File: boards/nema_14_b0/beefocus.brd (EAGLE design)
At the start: 82.2 x 44.4 mm, 24 parts, among them J3 POWER_JACK

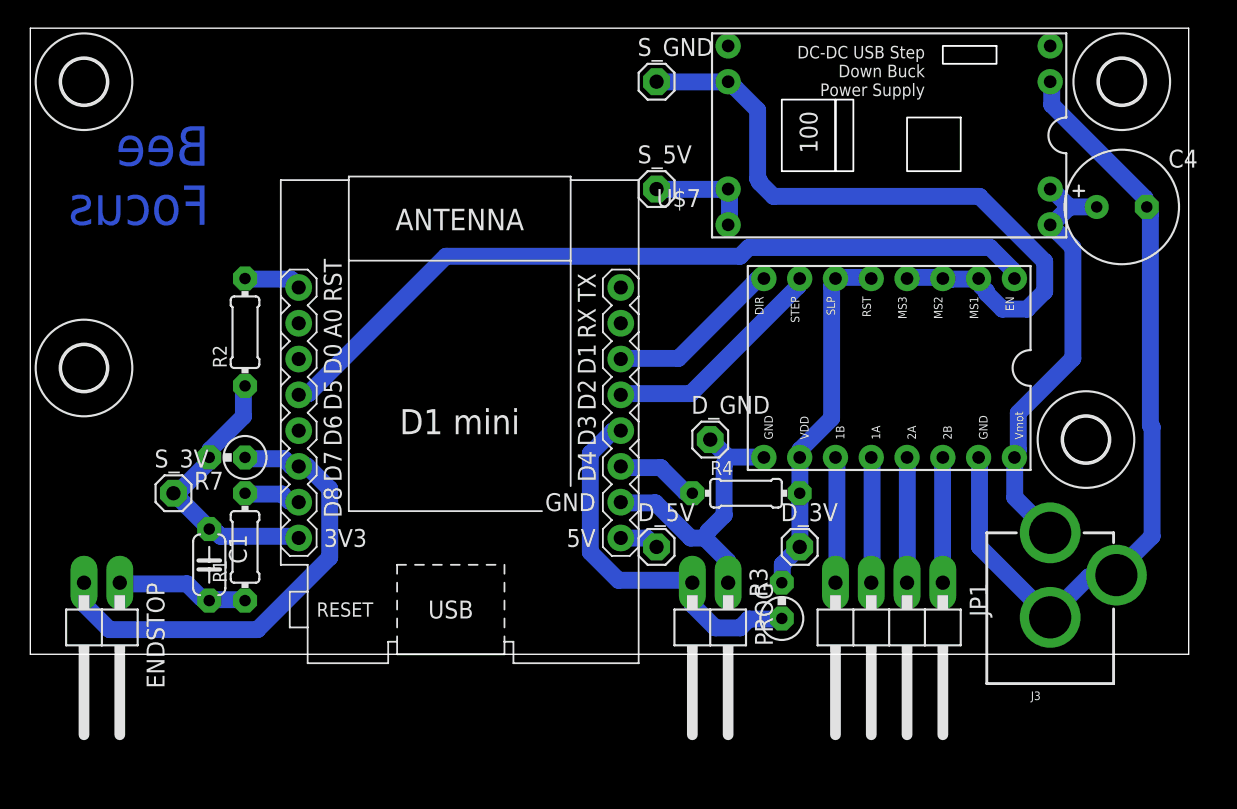
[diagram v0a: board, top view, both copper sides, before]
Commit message: Update board to fix lost trace to ground :(
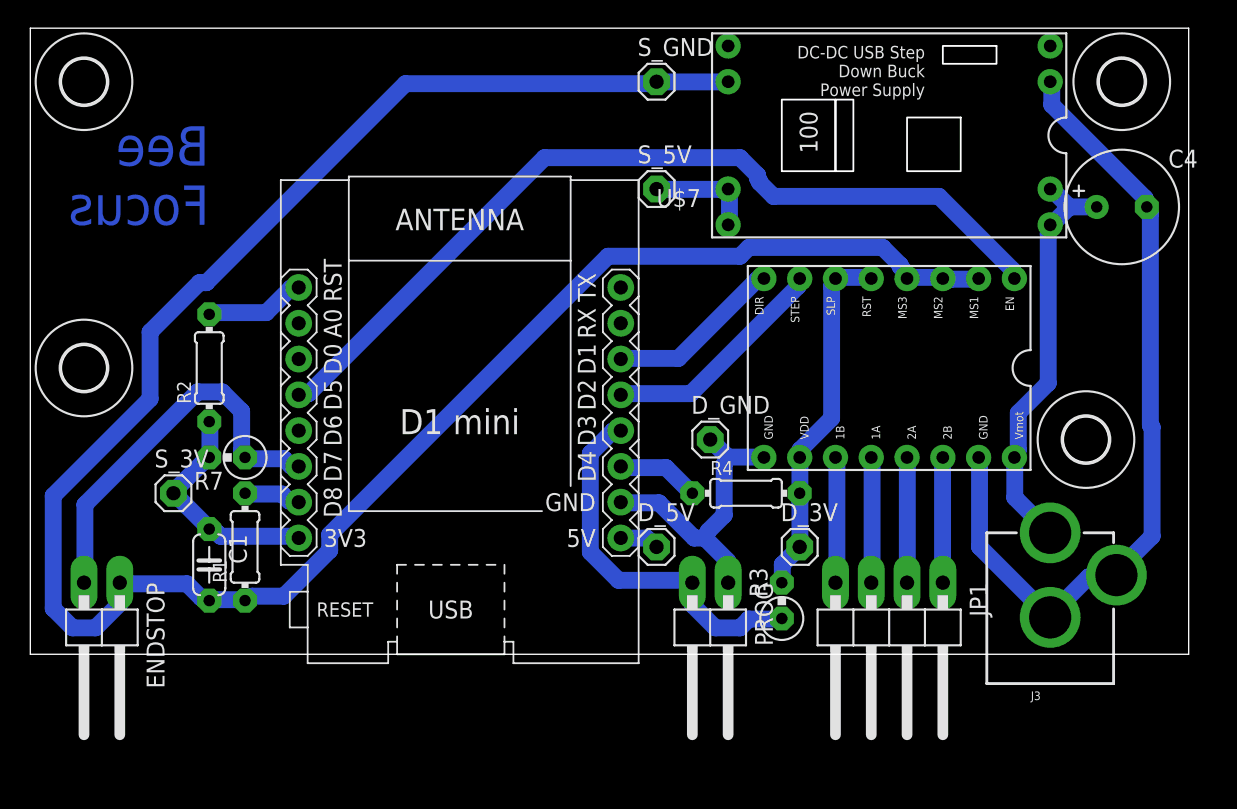
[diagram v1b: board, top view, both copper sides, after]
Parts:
- moved R2 3.59 mm to (12.7, 20.3)
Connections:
- removed net N$13: C1.2, ENDSTOP.1, R1.1
- net N$18: now also C1.2, ENDSTOP.1, R1.1
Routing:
- net N$18: track 49.4 -> 152.1 mm
- net N$13: track 9.44 -> 0.00 mm
- net N$20: track 33.7 -> 28.0 mm
- net N$11: track 56.3 -> 61.8 mm
- net N$22: track 20.0 -> 16.4 mm
- net N$14: track 4.11 -> 7.17 mm
- net N$9: track 31.0 -> 29.6 mm

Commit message: Update board to take a push button switch.  This will be used to do a hard reset in the future
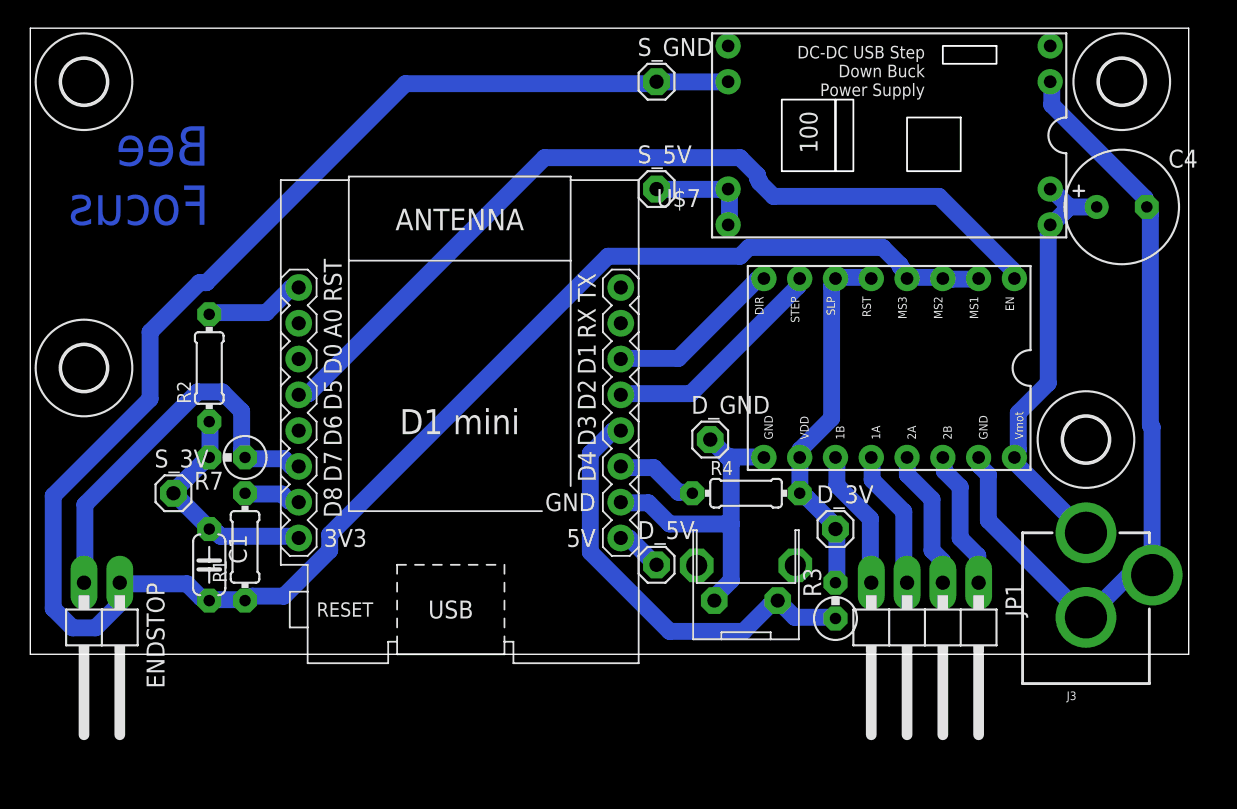
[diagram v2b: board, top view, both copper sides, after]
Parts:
- removed PROG: (no value), pinhead:1X02/90
- added U$8: BUTTON6X6X10MMSIDE, glowmouse_custom:BUTTON6X6X10MMSIDE
- moved R3 3.81 mm to (57.1, 3.81)
- moved D_3V 2.84 mm to (57.1, 8.89)
- moved J3 2.54 mm to (74.9, -5.08)
- moved JP1 2.54 mm to (63.5, 1.27)
- moved D_5V 1.27 mm to (44.5, 6.35)
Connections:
- net N$10: now also U$8.PB_P1; no longer PROG.2
- net N$16: now also U$8.PB_P0; no longer PROG.1
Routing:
- net N$10: track 26.8 -> 31.0 mm
- net N$16: track 21.5 -> 23.5 mm
- net N$9: track 29.6 -> 30.6 mm
- net N$5: track 8.90 -> 9.95 mm
- net N$6: track 8.90 -> 9.93 mm
- net N$7: track 8.94 -> 9.96 mm
- net N$8: track 9.00 -> 9.95 mm
- net N$17: track 25.7 -> 26.4 mm
- net N$2: track 2.80 -> 3.32 mm

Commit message: Change microstepping to 1/16th on board.
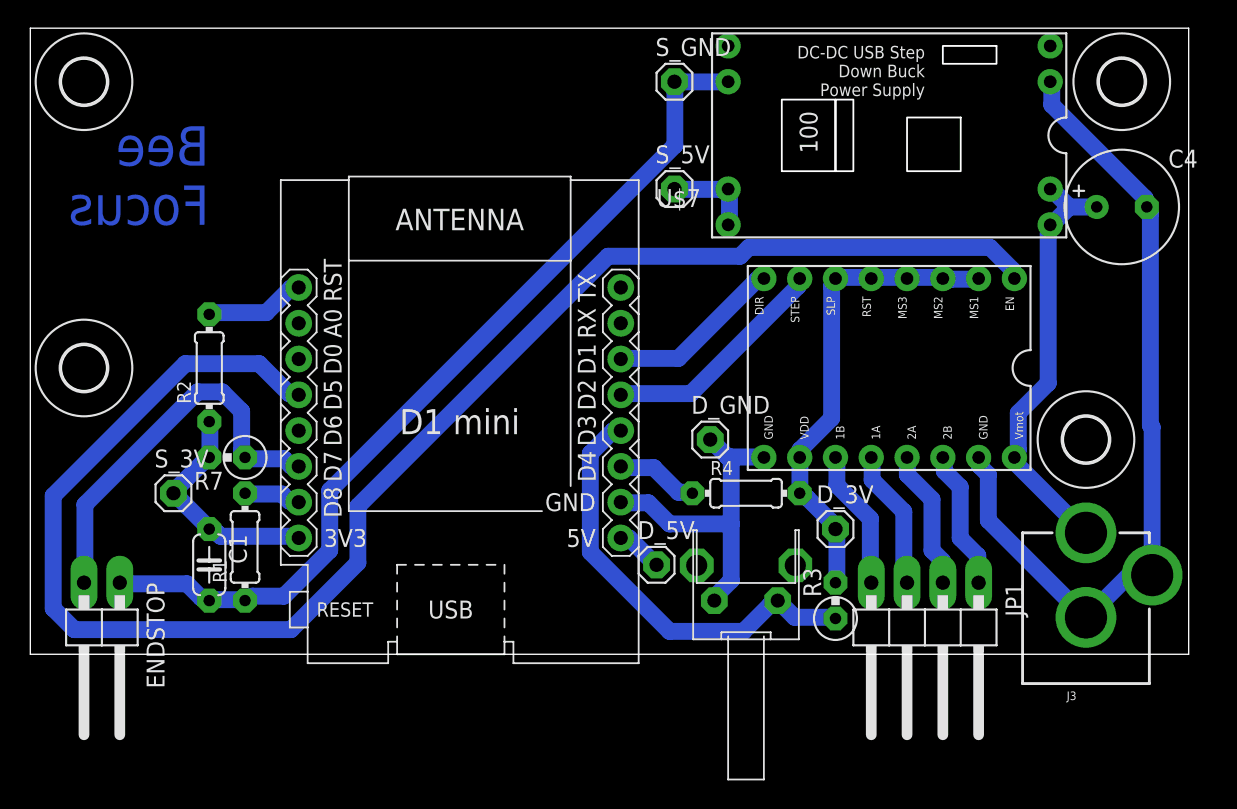
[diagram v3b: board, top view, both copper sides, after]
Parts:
- moved S_5V 1.27 mm to (45.7, 33.0)
- moved S_GND 1.27 mm to (45.7, 40.6)
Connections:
- net N$17: now also U$1.MS1, U$1.MS2, U$1.MS3
- net N$18: no longer U$1.MS1, U$1.MS2, U$1.MS3
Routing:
- net N$18: track 152.1 -> 64.1 mm
- net N$11: track 61.8 -> 113.9 mm
- net N$17: track 26.4 -> 34.2 mm
- net N$12: track 7.78 -> 6.51 mm
